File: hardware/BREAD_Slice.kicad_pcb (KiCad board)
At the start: 2 copper layers, 70 x 100 mm, 38 parts, among them J1 Conn_01x10_Socket, J2 Screw_Terminal_01x04, J3 Screw_Terminal_01x04, J4 Screw_Terminal_01x02, J5 Screw_Terminal_01x02, J6 Screw_Terminal_01x02, J7 Screw_Terminal_01x02, U1 AP63205, U2 LMD18200T_NOPB, U3 LMD18200T_NOPB

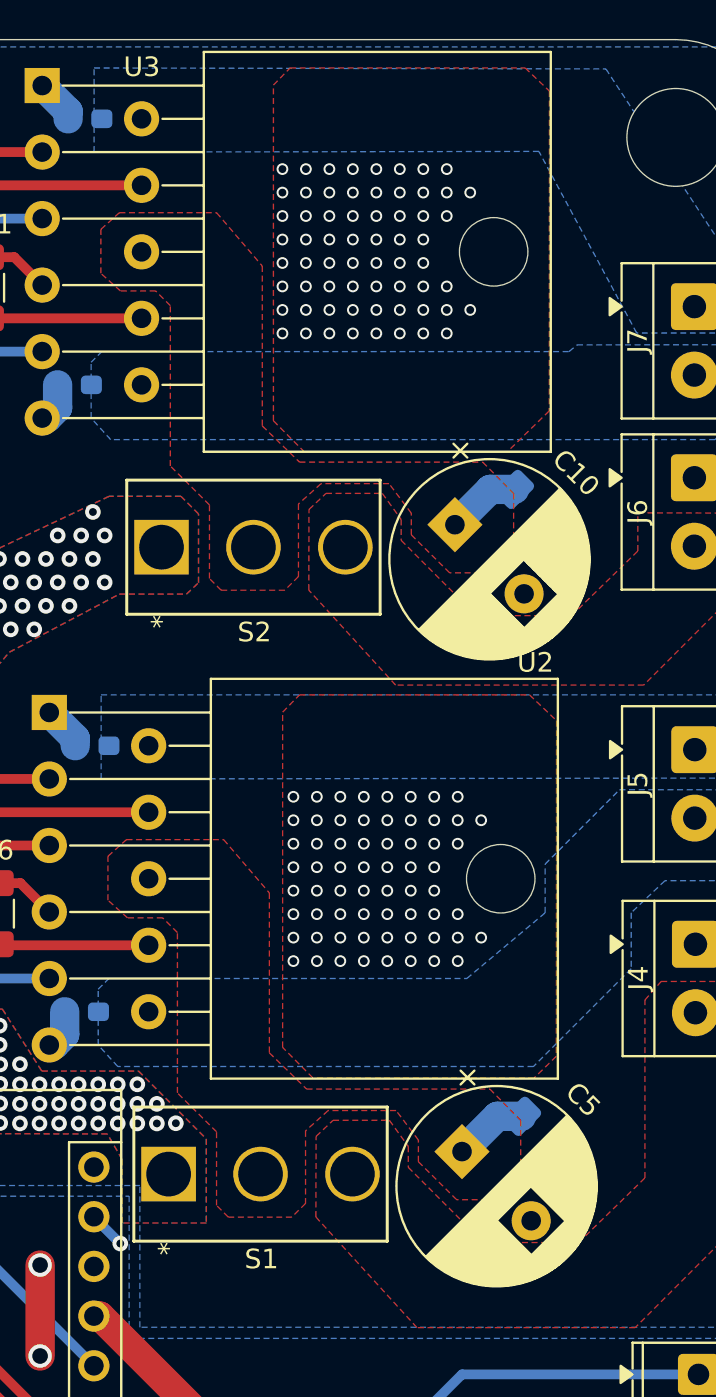
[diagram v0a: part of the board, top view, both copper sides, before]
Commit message: feat: update to kicad 10 and migrate old references to kml
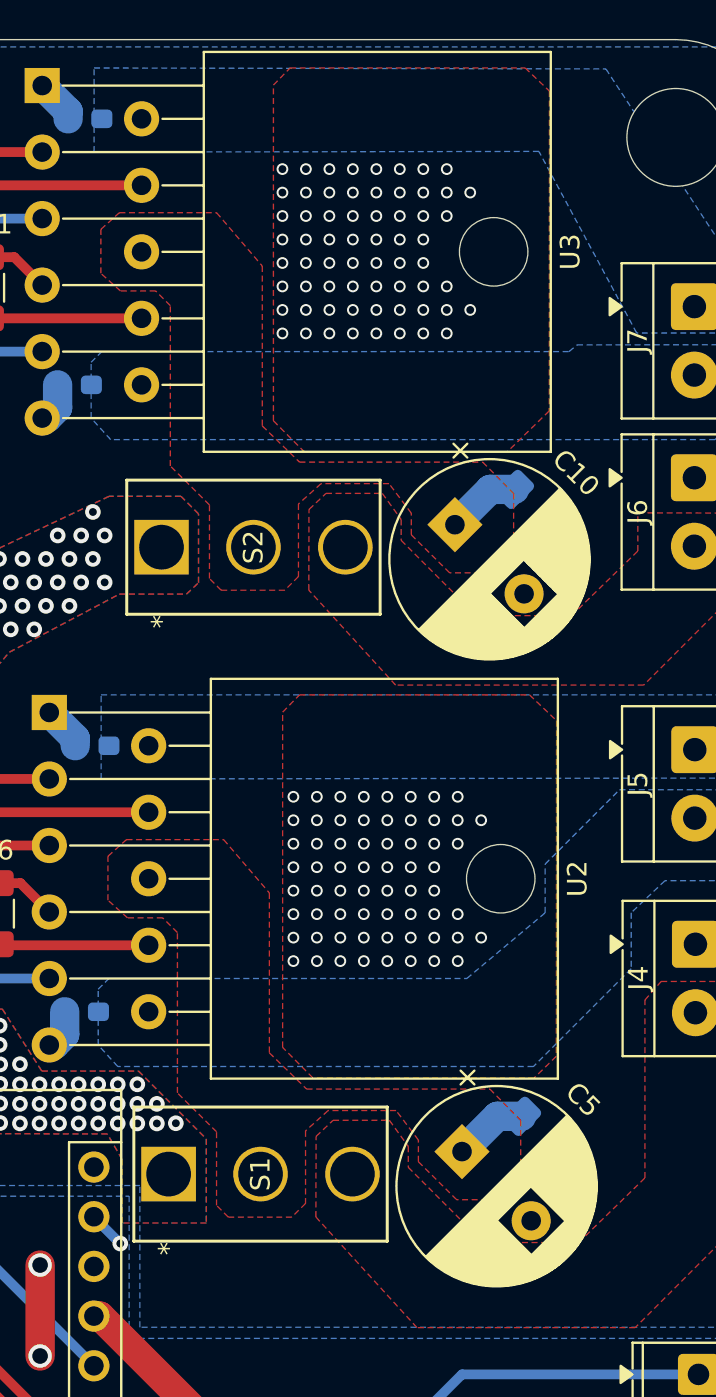
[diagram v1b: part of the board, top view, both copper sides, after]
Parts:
- HS1: footprint kml-custom:Thermal Pad -> KMLib_Mounting:Thermal_Pad
- S1, S2: footprint kml-custom:SW_Slide-CK-1101M2S3CQE2 -> KMLib_Switches:SW_Slide-CK-1101M2S3CQE2
- U1: footprint kml-custom:SOIC_05WU-7_DIO -> KMLib_IC_SMD:SOIC_05WU-7_DIO
- U2, U3: footprint Package_TO_SOT_THT:TO-220-11_P3.4x5.08mm_StaggerOdd_Lead8.45mm_TabDown -> KMLib_IC_THT:TO-220-11_P3.4x5.08mm_StaggerOdd_Lead8.45mm_TabDown
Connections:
- A1 pad 3: (no net) -> unconnected-(A1-~{RESET}-Pad3)

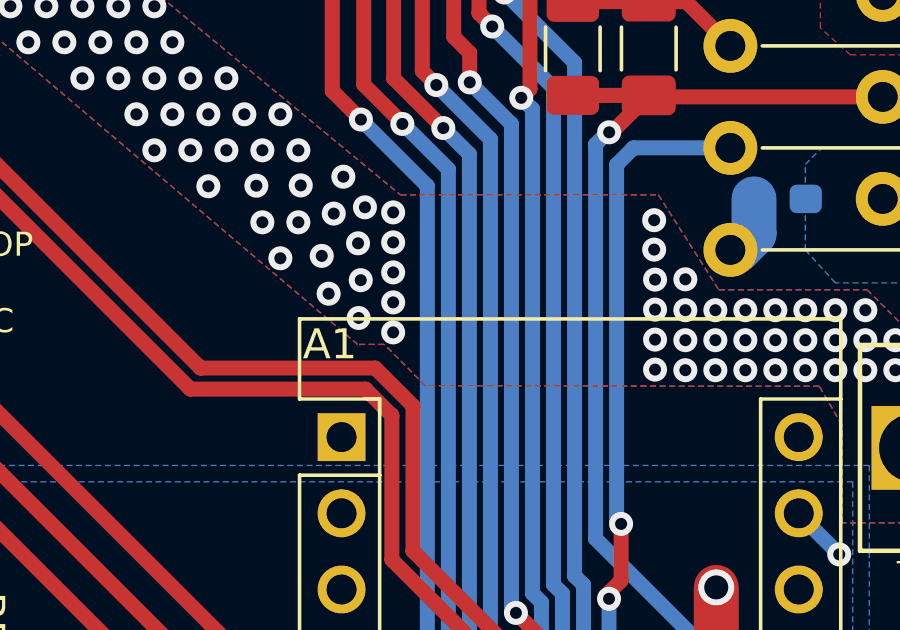
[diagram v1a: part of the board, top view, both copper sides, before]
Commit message: update ws2812 reference (was locked)
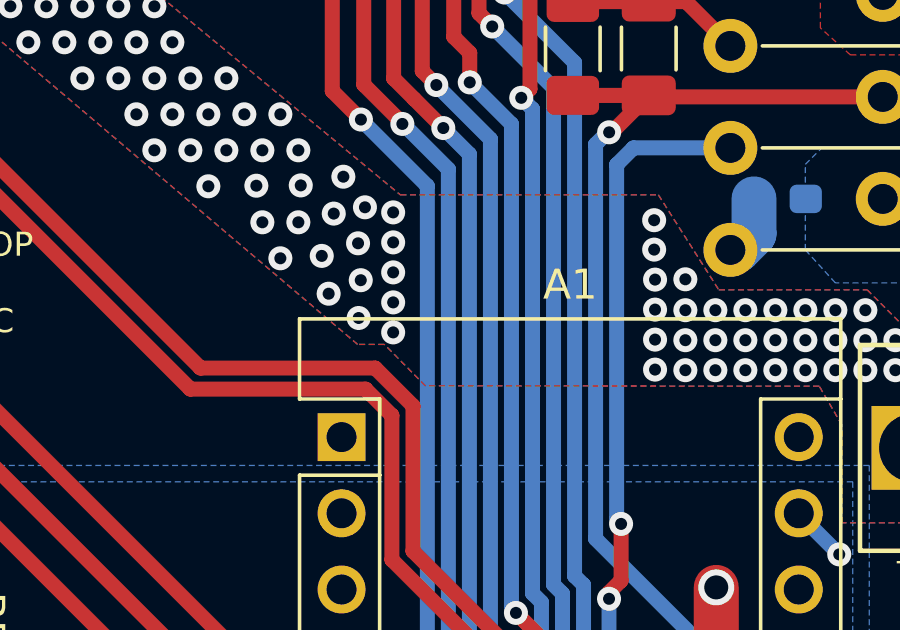
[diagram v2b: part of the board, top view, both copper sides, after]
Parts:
- A1: footprint KMLib_Boards_Modules:Arduino_Nano_Headers -> Module:Arduino_Nano
- D1: footprint SparkFun-LED:WS2812-5050-4PIN -> KMLib_IC_SMD:WS2812-5050-4PIN
